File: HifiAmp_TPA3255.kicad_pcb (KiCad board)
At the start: 4 copper layers, 200 x 150 mm, 124 parts, among them J1 PVDD 48V IN — NEEDS_DATA, J2 RCA L SE, J3 RCA R SE, J301 SPK_L, J302 SPK_R, J4 VOLUME_REMOTE, Q301 IPP330P10NM, Q302 IXTK200N10L2, U1 LM5010ASD, U2 LM2940IMP-12/NOPB, U3 TLV1117-33IDCY, U4 OPA1612AIDR, U5 OPA1612AIDR, U6 TPA3255B, U7 TPS3802K33DCKR, U8 LM5069-2

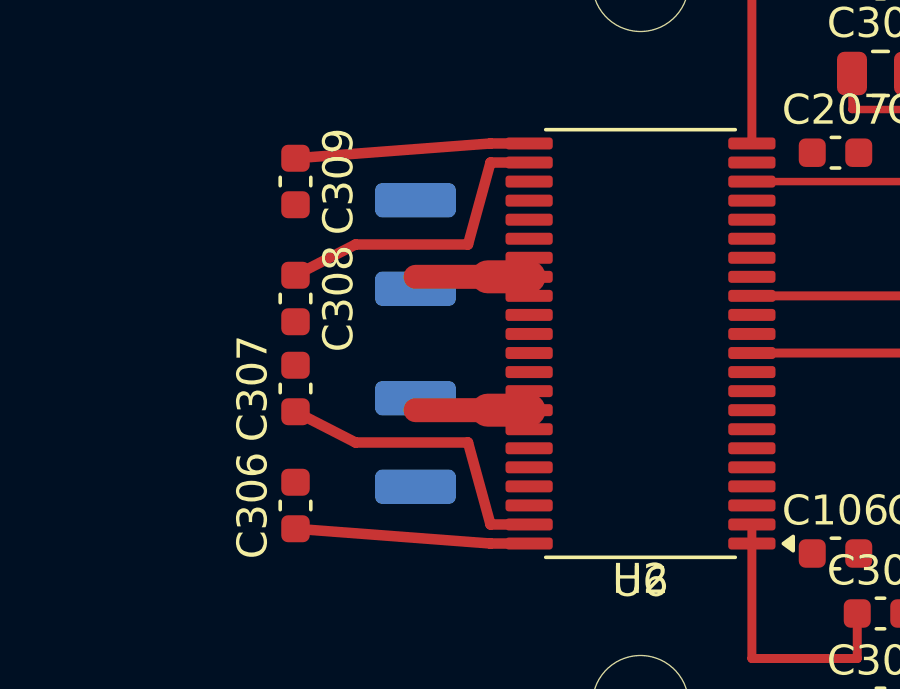
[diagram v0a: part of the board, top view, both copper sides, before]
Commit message: feat(f1.2-b1): reroute C310/C311 decoupling through four vias, loop criterion still open
C310/C311 are turned 180 deg on B.Cu so each pad faces its U6 pin; /PVDD and
/GND now reach U6 through four vias. DRC is clean (no clearance, shorting or
dangling), unconnected 232 -> 226, parity 3, 124 footprints, 119 (units.

Measured with F1.1's metric, the loop is ~10.8 mm against the 7.71 mm target:
the board crossings add to the planar path instead of replacing it. F1.2-b1
stays open pending a decision. Also records that the KiCad API had to be
enabled and that its socket is a named pipe on Windows.

Co-Authored-By: Claude Opus 5.5 <noreply@anthropic.com>
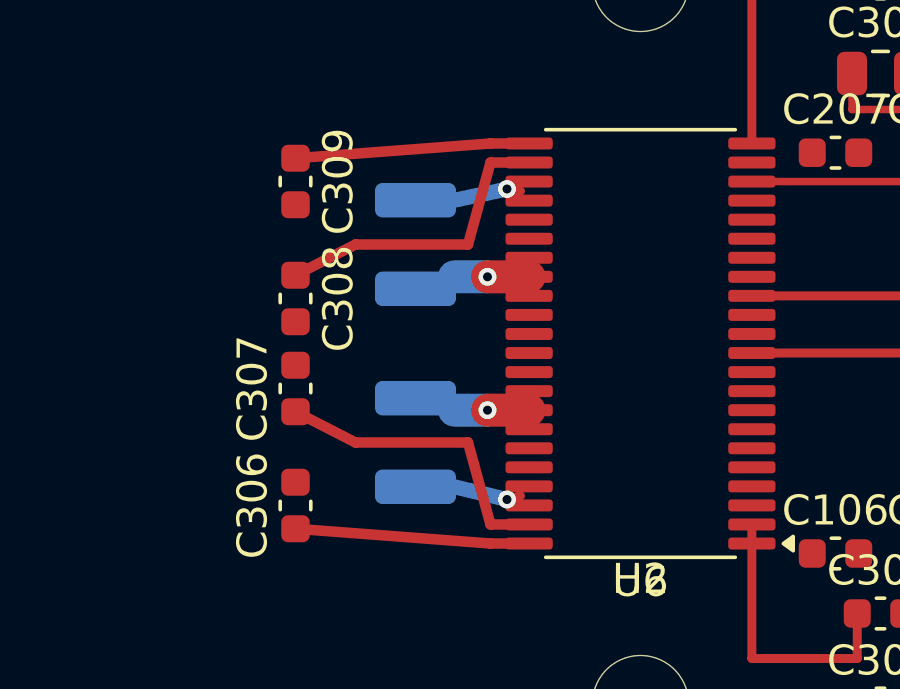
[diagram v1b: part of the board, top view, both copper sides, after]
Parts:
- turned C310 to -90 degrees
- turned C311 to 90 degrees
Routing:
- net /GND: track 0.00 -> 4.51 mm, vias 0 -> 2
- net /PVDD: track 7.58 -> 4.98 mm, vias 0 -> 2

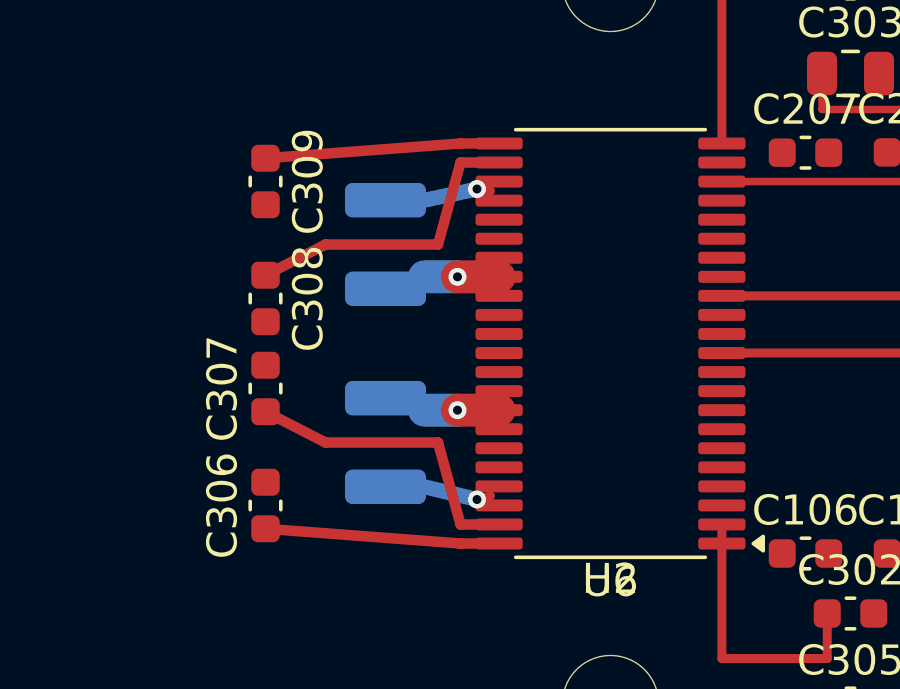
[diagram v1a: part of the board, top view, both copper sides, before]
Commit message: feat(f1.2-b1): slide C310/C311 under U6, decoupling loop 10.8 -> 9.63 mm
User decision: the 7.71 mm loop target cannot be met with vias, so the two
capacitors slide under U6 on B.Cu (x 280.75). Four tented vias at x 282.6,
under the package body and east of the pins, since BST_B/BST_C block the
west side for GND. 9.63 mm is the minimum without vias in pads.

DRC clean (clearance, shorting, dangling, courtyard all 0), unconnected 226,
parity 3, 124 footprints, 119 (units. F1.2-b1 checked with its revised loop
criterion; the free-column check moves to F1.2-b2.

Co-Authored-By: Claude Opus 5.5 <noreply@anthropic.com>
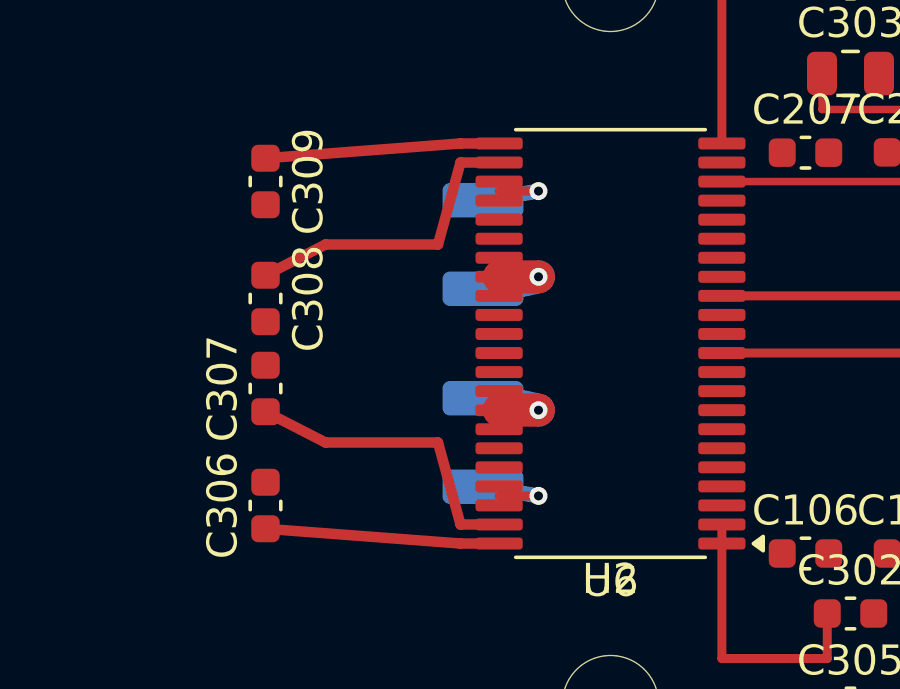
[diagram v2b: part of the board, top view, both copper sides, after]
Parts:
- moved C310 3.25 mm to (280.8, 178.3)
- moved C311 3.25 mm to (280.8, 171.7)
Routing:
- net /GND: track 4.51 -> 6.37 mm
- net /PVDD: track 4.98 -> 6.41 mm
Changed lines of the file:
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@@
 	(footprint "Capacitor_SMD:C_1210_3225Metric"
 		(layer "B.Cu")
-		(at 277.5 178.3 -90)
+		(at 280.75 178.3 -90)
 		(descr "Capacitor SMD 1210 (3225 Metric), square (rectangular) end terminal, IPC-7351 nominal, (Body size source: IPC-SM-782 page 76, https://www.pcb-3d.com/wordpress/wp-content/uploads/ipc-sm-782a_amendment_1_and_2.pdf)")
 		(tags "capacitor")
@@
 	(footprint "Capacitor_SMD:C_1210_3225Metric"
 		(layer "B.Cu")
-		(at 277.5 171.7 90)
+		(at 280.75 171.7 90)
 		(descr "Capacitor SMD 1210 (3225 Metric), square (rectangular) end terminal, IPC-7351 nominal, (Body size source: IPC-SM-782 page 76, https://www.pcb-3d.com/wordpress/wp-content/uploads/ipc-sm-782a_amendment_1_and_2.pdf)")
 		(tags "capacitor")
 		(property "Reference" "C311"
-			(at 0 2.3 -90)
+			(at 0 2.3 270)
 			(layer "B.SilkS")
 			(effects
@@
 		)
 		(property "Value" "1uF/100V"
-			(at 0 -2.3 -90)
+			(at 0 -2.3 270)
 			(layer "B.Fab")
 			(effects
@@
 		)
 		(property "Datasheet" ""
-			(at 0 0 -90)
+			(at 0 0 270)
 			(layer "B.Fab")
 			(hide yes)
@@
 		)
 		(property "Description" ""
-			(at 0 0 -90)
+			(at 0 0 270)
 			(layer "B.Fab")
 			(hide yes)
@@
 		)
 		(property "KiLib_Generator" "SMD_2terminal_chip_molded"
-			(at 0 0 -90)
+			(at 0 0 270)
 			(layer "B.SilkS")
 			(hide yes)
@@
 		)
 		(fp_text user "${REFERENCE}"
-			(at 0 0 -90)
+			(at 0 0 270)
 			(layer "B.Fab")
 			(effects
@@
 	)
 	(segment
-		(start 280.55 180.2)
-		(end 281 180.08)
-		(width 0.3)
-		(layer "F.Cu")
-		(net "/GND")
-	)
-	(segment
-		(start 280.55 169.85)
-		(end 281 169.92)
+		(start 282.6 180.08)
+		(end 281.2875 180.08)
+		(width 0.3)
+		(layer "F.Cu")
+		(net "/GND")
+	)
+	(segment
+		(start 282.6 169.92)
+		(end 281.2875 169.92)
 		(width 0.3)
 		(layer "F.Cu")
@@
 	)
 	(via
-		(at 280.55 180.2)
+		(at 282.6 180.08)
 		(size 0.6)
 		(drill 0.3)
@@
 	)
 	(via
-		(at 280.55 169.85)
+		(at 282.6 169.92)
 		(size 0.6)
 		(drill 0.3)
@@
 	)
 	(segment
-		(start 278.8 179.775)
-		(end 280.55 180.2)
+		(start 282.6 169.92)
+		(end 280.75 170.225)
 		(width 0.5)
 		(layer "B.Cu")
@@
 	)
 	(segment
-		(start 278.8 170.225)
-		(end 280.55 169.85)
+		(start 282.6 180.08)
+		(end 280.75 179.775)
 		(width 0.5)
 		(layer "B.Cu")
@@
 	)
 	(segment
-		(start 279.9 177.2225)
-		(end 281.2875 177.2225)
+		(start 281.2875 177.2225)
+		(end 282.6 177.2225)
 		(width 1.1)
 		(layer "F.Cu")
@@
 	)
 	(segment
-		(start 279.9 172.7775)
-		(end 281.2875 172.7775)
+		(start 281.2875 172.7775)
+		(end 282.6 172.7775)
 		(width 1.1)
 		(layer "F.Cu")
@@
 	)
 	(via
-		(at 279.9 172.7775)
+		(at 282.6 172.7775)
 		(size 0.6)
 		(drill 0.3)
@@
 	)
 	(via
-		(at 279.9 177.2225)
+		(at 282.6 177.2225)
 		(size 0.6)
 		(drill 0.3)
@@
 	)
 	(segment
-		(start 278.8 172.7775)
-		(end 279.9 172.7775)
+		(start 282.6 172.7775)
+		(end 280.75 173.175)
 		(width 1.1)
 		(layer "B.Cu")
@@
 	)
 	(segment
-		(start 278.8 177.2225)
-		(end 279.9 177.2225)
+		(start 282.6 177.2225)
+		(end 280.75 176.825)
 		(width 1.1)
 		(layer "B.Cu")

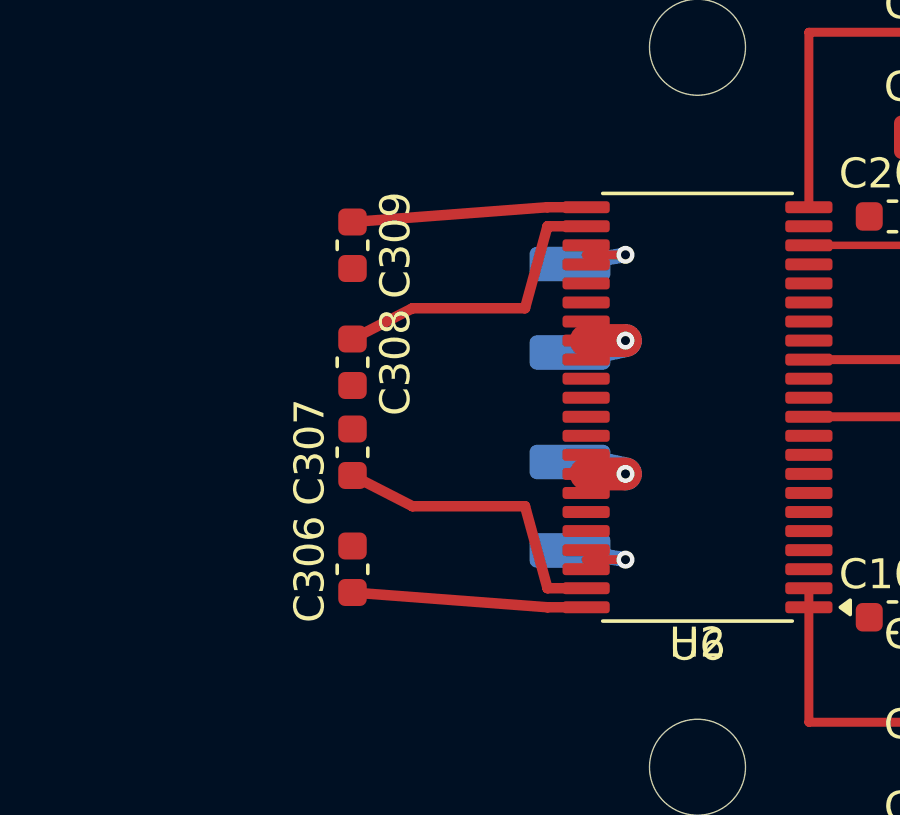
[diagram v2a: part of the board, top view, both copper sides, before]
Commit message: feat(f1.2-b2): take BST_B/BST_C under the OUT row, free the escape column
BST_B and BST_C dive to B.Cu with two vias each: a net that starts on an F.Cu
pin and ends on an F.Cu SMD pad needs an even via count, so the planned
"one via each" is revised to four in total. BST_A and BST_D go around on
F.Cu at y 182.4 and 167.6 without vias. All at 0.35 mm.

The F.Cu column x 276.15-278.85, y 168-182 is now empty. DRC unchanged:
no clearance, shorting, dangling or courtyard errors, parity 3, unconnected
226. Only the /BST_A../BST_D nets changed, no footprint touched.

Co-Authored-By: Claude Opus 5.5 <noreply@anthropic.com>
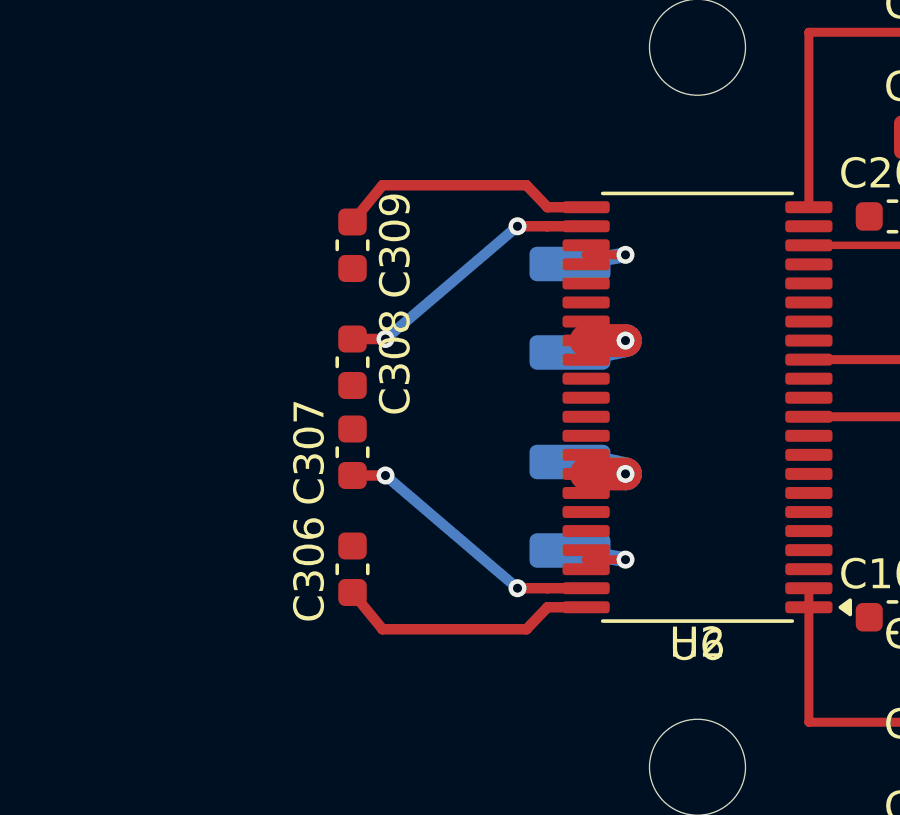
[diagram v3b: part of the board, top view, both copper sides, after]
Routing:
- net /BST_B: track 10.1 -> 9.17 mm, vias 0 -> 2
- net /BST_C: track 10.1 -> 9.17 mm, vias 0 -> 2
- net /BST_D: track 7.81 -> 8.68 mm
- net /BST_A: track 7.81 -> 8.68 mm
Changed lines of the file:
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@@
+	)
+	(segment
+		(start 279.3 167.6)
+		(end 274.5 167.6)
+		(width 0.35)
+		(layer "F.Cu")
+		(net "/BST_D")
+	)
+	(segment
+		(start 280 168.3325)
+		(end 279.3 167.6)
+		(width 0.35)
+		(layer "F.Cu")
+		(net "/BST_D")
+	)
+	(segment
+		(start 274.5 167.6)
+		(end 273.5 168.825)
+		(width 0.35)
+		(layer "F.Cu")
+		(net "/BST_D")
 	)
 	(segment
@@
 	)
 	(segment
-		(start 280 168.3325)
-		(end 273.5 168.825)
-		(width 0.35)
-		(layer "F.Cu")
-		(net "/BST_D")
-	)
-	(segment
-		(start 279.25 171.7)
-		(end 275.5 171.7)
+		(start 280 168.9675)
+		(end 279 168.9675)
 		(width 0.35)
 		(layer "F.Cu")
@@
 	)
 	(segment
-		(start 275.5 171.7)
+		(start 274.6 172.725)
 		(end 273.5 172.725)
 		(width 0.35)
@@
 		(net "/BST_C")
 	)
-	(segment
-		(start 280 168.9675)
-		(end 279.25 171.7)
-		(width 0.35)
-		(layer "F.Cu")
+	(via
+		(at 274.6 172.725)
+		(size 0.6)
+		(drill 0.3)
+		(layers "F.Cu" "B.Cu")
+		(net "/BST_C")
+	)
+	(via
+		(at 279 168.9675)
+		(size 0.6)
+		(drill 0.3)
+		(layers "F.Cu" "B.Cu")
 		(net "/BST_C")
 	)
 	(segment
-		(start 275.5 178.3)
-		(end 273.5 177.275)
+		(start 279 168.9675)
+		(end 274.6 172.725)
 		(width 0.35)
-		(layer "F.Cu")
-		(net "/BST_B")
+		(layer "B.Cu")
+		(net "/BST_C")
 	)
 	(segment
@@
 	(segment
 		(start 280 181.0325)
-		(end 279.25 178.3)
+		(end 279 181.0325)
 		(width 0.35)
 		(layer "F.Cu")
@@
 	)
 	(segment
-		(start 279.25 178.3)
-		(end 275.5 178.3)
+		(start 274.6 177.275)
+		(end 273.5 177.275)
 		(width 0.35)
 		(layer "F.Cu")
+		(net "/BST_B")
+	)
+	(via
+		(at 274.6 177.275)
+		(size 0.6)
+		(drill 0.3)
+		(layers "F.Cu" "B.Cu")
+		(net "/BST_B")
+	)
+	(via
+		(at 279 181.0325)
+		(size 0.6)
+		(drill 0.3)
+		(layers "F.Cu" "B.Cu")
+		(net "/BST_B")
+	)
+	(segment
+		(start 279 181.0325)
+		(end 274.6 177.275)
+		(width 0.35)
+		(layer "B.Cu")
 		(net "/BST_B")
 	)
@@
 	)
 	(segment
+		(start 279.3 182.4)
+		(end 274.5 182.4)
+		(width 0.35)
+		(layer "F.Cu")
+		(net "/BST_A")
+	)
+	(segment
 		(start 280 181.6675)
+		(end 279.3 182.4)
+		(width 0.35)
+		(layer "F.Cu")
+		(net "/BST_A")
+	)
+	(segment
+		(start 274.5 182.4)
 		(end 273.5 181.175)
 		(width 0.35)

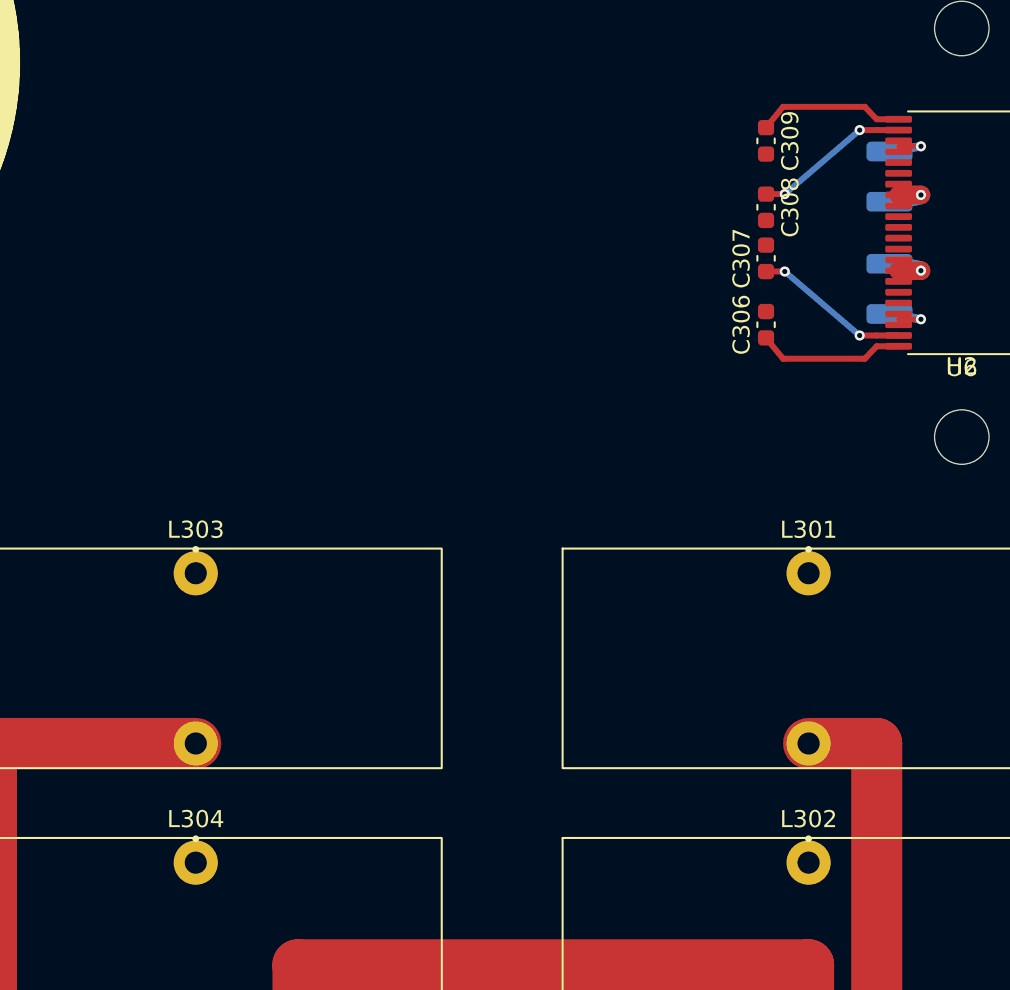
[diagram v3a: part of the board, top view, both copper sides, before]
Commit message: feat(f1.2-b3): route OUT_A..OUT_D to bootstraps and inductors, width criterion open
All four switching nodes are routed on F.Cu without vias: unconnected
226 -> 216, DRC clean, parity 3. The U6 escape DRU rule is shown to be
selective: with U6 removed from its condition, 14 clearance errors appear,
all OUT track to U6 pad, and none elsewhere.

Left open: about 12 mm per net stays below 3.00 mm, partly outside the fine
pitch (0.96-1.07 mm necks between the bootstrap pads), and OUT_D runs
101 mm because L303/L304 sit 45 mm from U6. Pending a placement decision.

Co-Authored-By: Claude Opus 5.5 <noreply@anthropic.com>
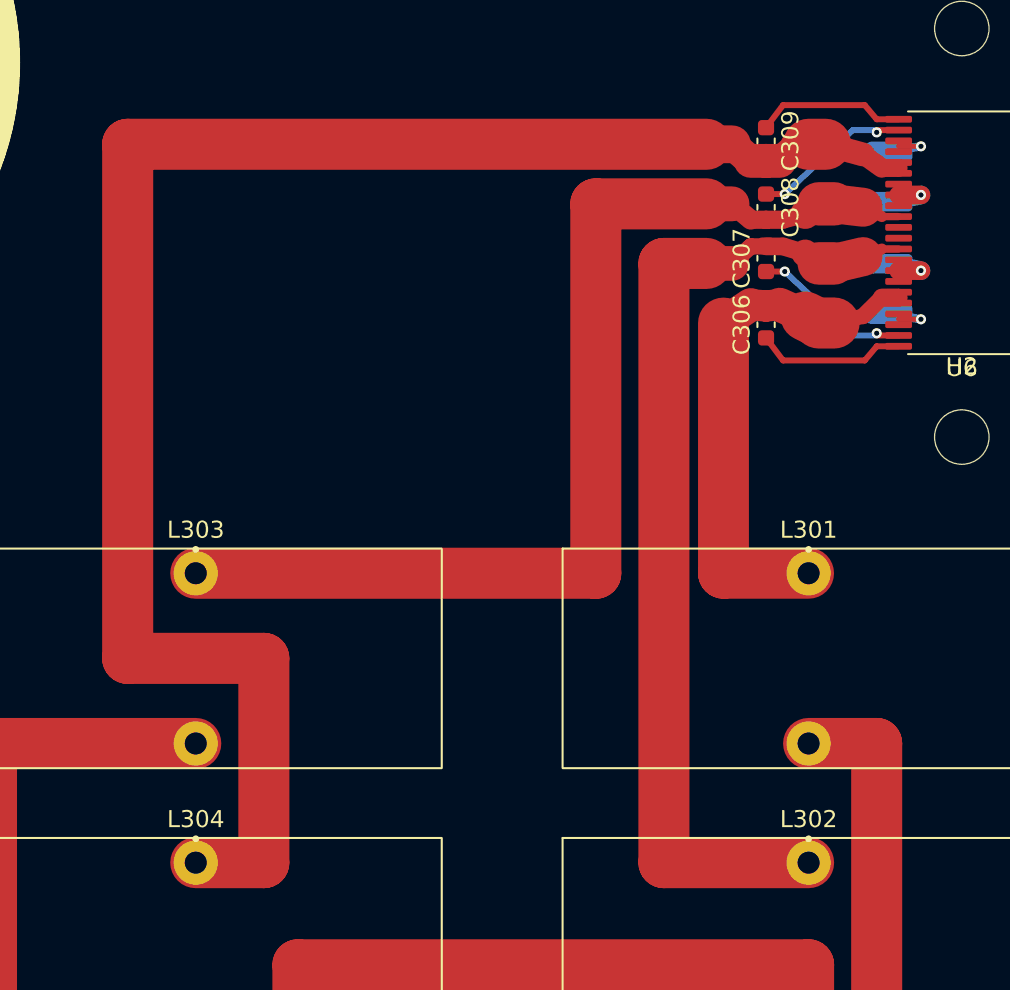
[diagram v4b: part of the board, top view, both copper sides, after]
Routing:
- net /OUT_D: track 0.00 -> 101.2 mm
- net /OUT_C: track 0.00 -> 63.7 mm
- net /OUT_B: track 0.00 -> 58.3 mm
- net /OUT_A: track 0.00 -> 31.7 mm
